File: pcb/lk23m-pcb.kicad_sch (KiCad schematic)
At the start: 59 parts, among them J1 Conn_01x02, SW1 RotaryEncoder_Switch_MP, SW10 SW_Push, SW11 SW_Push, SW12 SW_Push, SW13 SW_Push, SW14 SW_Push, SW15 SW_Push, SW16 SW_Push, SW17 SW_Push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

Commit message: Update LKBD libraries
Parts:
- H1, H2, H3, H4: value MountingHole -> MountingHole_Pad
- SW24: footprint LKBD_Common:SW_PUSH_1P1T_6x3.5mm -> LKBD_Common:SW_Push_1P1T_6x3.5mm
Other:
- moved on the sheet: H1, H2, H3, H4
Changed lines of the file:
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@@
 	)
 	(no_connect
-		(at 48.26 77.47)
+		(at 44.45 77.47)
 	)
 	(no_connect
@@
 	)
 	(no_connect
-		(at 26.67 77.47)
+		(at 20.32 77.47)
 	)
 	(no_connect
-		(at 91.44 77.47)
+		(at 92.71 77.47)
 	)
 	(no_connect
@@
 	)
 	(no_connect
-		(at 69.85 77.47)
+		(at 68.58 77.47)
 	)
 	(wire
@@
 	(symbol
 		(lib_id "Mechanical:MountingHole_Pad")
-		(at 69.85 74.93 0)
+		(at 68.58 74.93 0)
 		(unit 1)
 		(exclude_from_sim yes)
@@
 		(dnp no)
 		(property "Reference" "H3"
-			(at 72.39 73.6599 0)
+			(at 71.12 73.6599 0)
 			(effects
 				(font
@@
 			)
 		)
-		(property "Value" "MountingHole"
-			(at 72.39 76.1999 0)
+		(property "Value" "MountingHole_Pad"
+			(at 71.12 76.1999 0)
 			(effects
 				(font
@@
 		)
 		(property "Footprint" "MountingHole:MountingHole_2.2mm_M2_ISO14580_Pad"
-			(at 69.85 74.93 0)
+			(at 68.58 74.93 0)
 			(effects
 				(font
@@
 		)
 		(property "Datasheet" "~"
-			(at 69.85 74.93 0)
+			(at 68.58 74.93 0)
 			(effects
 				(font
@@
 		)
 		(property "Description" "Mounting Hole with connection"
-			(at 69.85 74.93 0)
+			(at 68.58 74.93 0)
 			(effects
 				(font
@@
 		)
 		(property "LCSC" ""
-			(at 69.85 74.93 0)
+			(at 68.58 74.93 0)
 			(effects
 				(font
@@
 		)
 		(property "JLC" ""
-			(at 69.85 74.93 0)
+			(at 68.58 74.93 0)
 			(effects
 				(font
@@
 		)
 		(property "JLCPosOffset" ""
-			(at 69.85 74.93 0)
+			(at 68.58 74.93 0)
 			(effects
 				(font
@@
 		)
 		(property "JLCRotOffset" ""
-			(at 69.85 74.93 0)
+			(at 68.58 74.93 0)
 			(effects
 				(font
@@
 	(symbol
 		(lib_id "Mechanical:MountingHole_Pad")
-		(at 26.67 74.93 0)
+		(at 20.32 74.93 0)
 		(unit 1)
 		(exclude_from_sim yes)
@@
 		(dnp no)
 		(property "Reference" "H1"
-			(at 29.21 73.66 0)
+			(at 22.86 73.66 0)
 			(effects
 				(font
@@
 			)
 		)
-		(property "Value" "MountingHole"
-			(at 29.21 76.2 0)
+		(property "Value" "MountingHole_Pad"
+			(at 22.86 76.2 0)
 			(effects
 				(font
@@
 		)
 		(property "Footprint" "MountingHole:MountingHole_2.2mm_M2_ISO14580_Pad"
-			(at 26.67 74.93 0)
+			(at 20.32 74.93 0)
 			(effects
 				(font
@@
 		)
 		(property "Datasheet" "~"
-			(at 26.67 74.93 0)
+			(at 20.32 74.93 0)
 			(effects
 				(font
@@
 		)
 		(property "Description" "Mounting Hole with connection"
-			(at 26.67 74.93 0)
+			(at 20.32 74.93 0)
 			(effects
 				(font
@@
 		)
 		(property "LCSC" ""
-			(at 26.67 74.93 0)
+			(at 20.32 74.93 0)
 			(effects
 				(font
@@
 		)
 		(property "JLC" ""
-			(at 26.67 74.93 0)
+			(at 20.32 74.93 0)
 			(effects
 				(font
@@
 		)
 		(property "JLCPosOffset" ""
-			(at 26.67 74.93 0)
+			(at 20.32 74.93 0)
 			(effects
 				(font
@@
 		)
 		(property "JLCRotOffset" ""
-			(at 26.67 74.93 0)
+			(at 20.32 74.93 0)
 			(effects
 				(font
@@
 	(symbol
 		(lib_id "Mechanical:MountingHole_Pad")
-		(at 91.44 74.93 0)
+		(at 92.71 74.93 0)
 		(unit 1)
 		(exclude_from_sim yes)
@@
 		(dnp no)
 		(property "Reference" "H4"
-			(at 93.98 73.66 0)
+			(at 95.25 73.66 0)
 			(effects
 				(font
@@
 			)
 		)
-		(property "Value" "MountingHole"
-			(at 93.98 76.2 0)
+		(property "Value" "MountingHole_Pad"
+			(at 95.25 76.2 0)
 			(effects
 				(font
@@
 		)
 		(property "Footprint" "MountingHole:MountingHole_2.2mm_M2_ISO14580_Pad"
-			(at 91.44 74.93 0)
+			(at 92.71 74.93 0)
 			(effects
 				(font
@@
 		)
 		(property "Datasheet" "~"
-			(at 91.44 74.93 0)
+			(at 92.71 74.93 0)
 			(effects
 				(font
@@
 		)
 		(property "Description" "Mounting Hole with connection"
-			(at 91.44 74.93 0)
+			(at 92.71 74.93 0)
 			(effects
 				(font
@@
 		)
 		(property "LCSC" ""
-			(at 91.44 74.93 0)
+			(at 92.71 74.93 0)
 			(effects
 				(font
@@
 		)
 		(property "JLC" ""
-			(at 91.44 74.93 0)
+			(at 92.71 74.93 0)
 			(effects
 				(font
@@
 		)
 		(property "JLCPosOffset" ""
-			(at 91.44 74.93 0)
+			(at 92.71 74.93 0)
 			(effects
 				(font
@@
 		)
 		(property "JLCRotOffset" ""
-			(at 91.44 74.93 0)
+			(at 92.71 74.93 0)
 			(effects
 				(font
@@
 			)
 		)
-		(property "Footprint" "LKBD_Common:SW_PUSH_1P1T_6x3.5mm"
+		(property "Footprint" "LKBD_Common:SW_Push_1P1T_6x3.5mm"
 			(at 38.1 88.9 0)
 			(effects
@@
 	(symbol
 		(lib_id "Mechanical:MountingHole_Pad")
-		(at 48.26 74.93 0)
+		(at 44.45 74.93 0)
 		(unit 1)
 		(exclude_from_sim yes)
@@
 		(dnp no)
 		(property "Reference" "H2"
-			(at 50.8 73.66 0)
+			(at 46.99 73.66 0)
 			(effects
 				(font
@@
 			)
 		)
-		(property "Value" "MountingHole"
-			(at 50.8 76.2 0)
+		(property "Value" "MountingHole_Pad"
+			(at 46.99 76.2 0)
 			(effects
 				(font
@@
 		)
 		(property "Footprint" "MountingHole:MountingHole_2.2mm_M2_ISO14580_Pad"
-			(at 48.26 74.93 0)
+			(at 44.45 74.93 0)
 			(effects
 				(font
@@
 		)
 		(property "Datasheet" "~"
-			(at 48.26 74.93 0)
+			(at 44.45 74.93 0)
 			(effects
 				(font
@@
 		)
 		(property "Description" "Mounting Hole with connection"
-			(at 48.26 74.93 0)
+			(at 44.45 74.93 0)
 			(effects
 				(font
@@
 		)
 		(property "LCSC" ""
-			(at 48.26 74.93 0)
+			(at 44.45 74.93 0)
 			(effects
 				(font
@@
 		)
 		(property "JLC" ""
-			(at 48.26 74.93 0)
+			(at 44.45 74.93 0)
 			(effects
 				(font
@@
 		)
 		(property "JLCPosOffset" ""
-			(at 48.26 74.93 0)
+			(at 44.45 74.93 0)
 			(effects
 				(font
@@
 		)
 		(property "JLCRotOffset" ""
-			(at 48.26 74.93 0)
+			(at 44.45 74.93 0)
 			(effects
 				(font
@@
 					(size 1.524 1.524)
 				)
+				(hide yes)
 			)
 		)

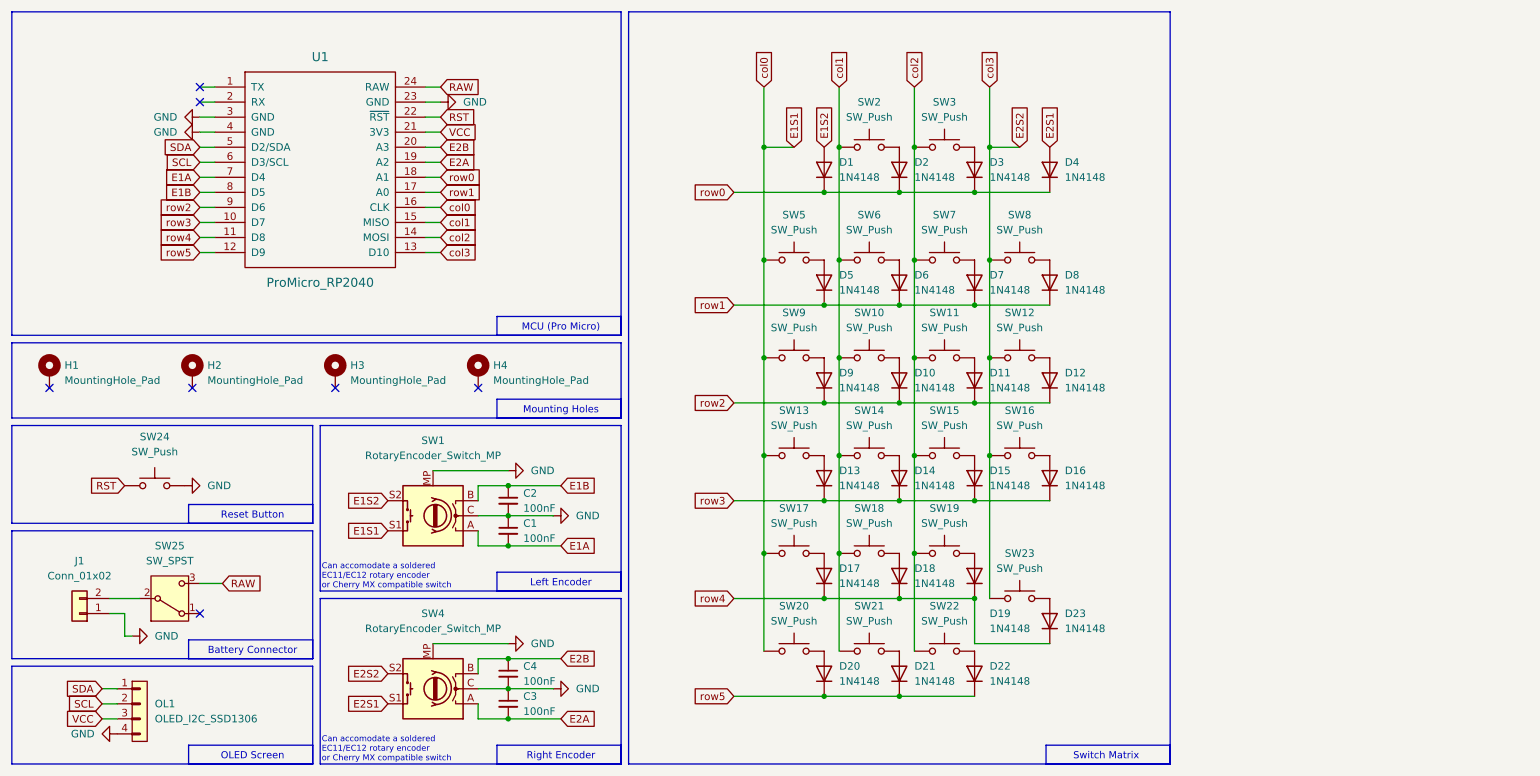
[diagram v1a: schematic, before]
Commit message: Update LICENSE document to Markdown
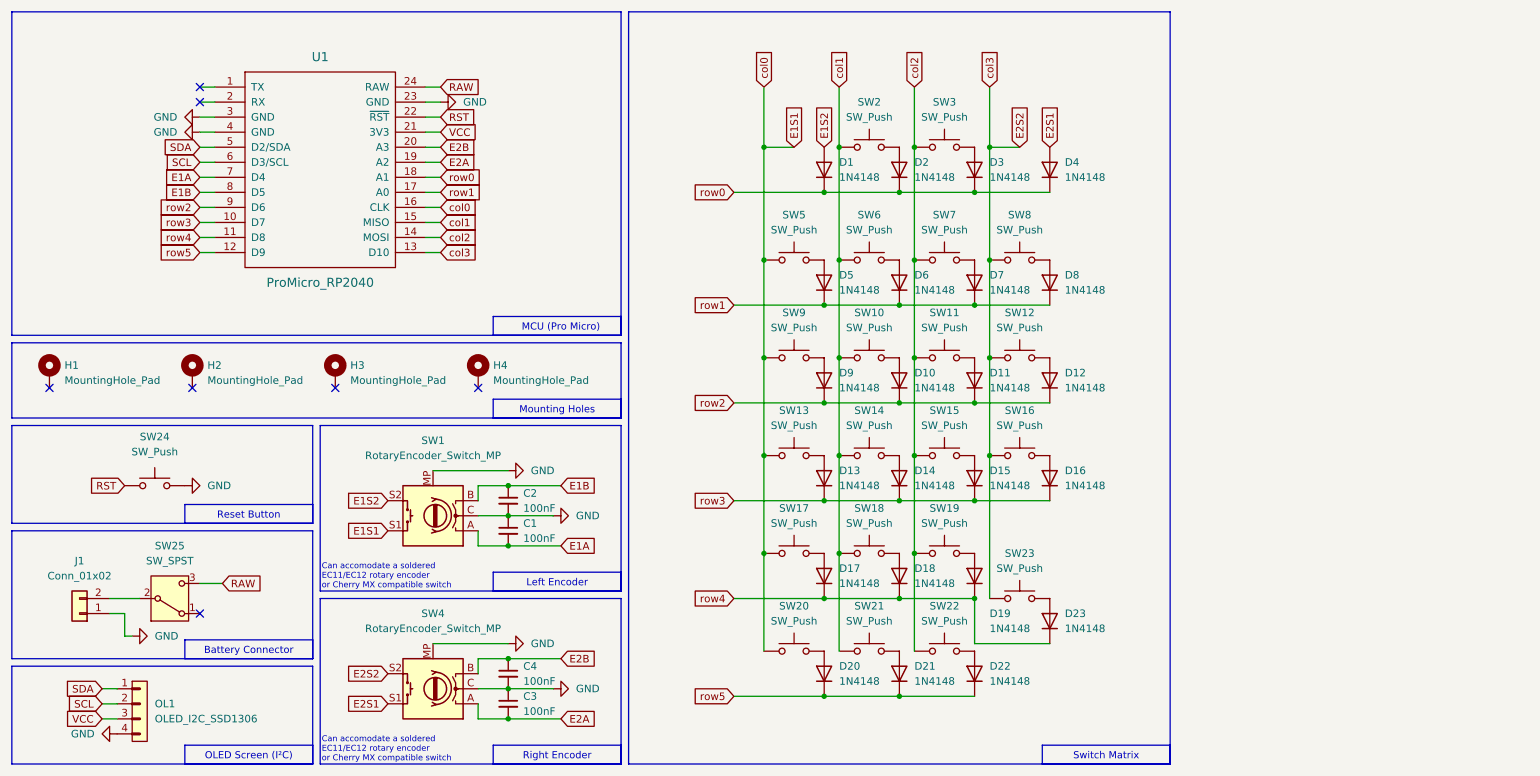
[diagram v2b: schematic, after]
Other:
- note added: "OLED Screen (I²C)"
- note removed: "OLED Screen"
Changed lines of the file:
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@@
+	)
+	(rectangle
+		(start 43.18 137.795)
+		(end 64.77 140.97)
+		(stroke
+			(width 0)
+			(type default)
+		)
+		(fill
+			(type none)
+		)
+	)
+	(rectangle
+		(start 95.25 108.585)
+		(end 116.84 111.76)
+		(stroke
+			(width 0)
+			(type default)
+		)
+		(fill
+			(type none)
+		)
+	)
+	(rectangle
+		(start 95.25 137.795)
+		(end 116.84 140.97)
+		(stroke
+			(width 0)
+			(type default)
+		)
+		(fill
+			(type none)
+		)
 	)
 	(rectangle
@@
 	)
 	(rectangle
-		(start 95.885 79.375)
+		(start 95.25 79.375)
 		(end 116.84 82.55)
 		(stroke
@@
 	)
 	(rectangle
-		(start 43.815 120.015)
-		(end 64.77 123.19)
-		(stroke
-			(width 0)
-			(type default)
-		)
-		(fill
-			(type none)
-		)
-	)
-	(rectangle
 		(start 13.97 13.97)
 		(end 116.84 68.58)
@@
 	)
 	(rectangle
-		(start 43.815 97.155)
+		(start 43.18 120.015)
+		(end 64.77 123.19)
+		(stroke
+			(width 0)
+			(type default)
+		)
+		(fill
+			(type none)
+		)
+	)
+	(rectangle
+		(start 43.18 97.155)
 		(end 64.77 100.33)
 		(stroke
@@
 	)
 	(rectangle
-		(start 188.595 137.795)
+		(start 187.96 137.795)
 		(end 209.55 140.97)
-		(stroke
-			(width 0)
-			(type default)
-		)
-		(fill
-			(type none)
-		)
-	)
-	(rectangle
-		(start 43.815 137.795)
-		(end 64.77 140.97)
 		(stroke
 			(width 0)
@@
 	)
 	(rectangle
-		(start 95.885 137.795)
-		(end 116.84 140.97)
-		(stroke
-			(width 0)
-			(type default)
-		)
-		(fill
-			(type none)
-		)
-	)
-	(rectangle
 		(start 13.97 83.82)
 		(end 64.77 100.33)
@@
 	)
 	(rectangle
-		(start 95.885 108.585)
-		(end 116.84 111.76)
-		(stroke
-			(width 0)
-			(type default)
-		)
-		(fill
-			(type none)
-		)
-	)
-	(rectangle
-		(start 95.885 65.405)
+		(start 95.25 65.405)
 		(end 116.84 68.58)
 		(stroke
@@
 	(text "Mounting Holes"
 		(exclude_from_sim no)
-		(at 106.68 81.28 0)
-		(effects
-			(font
-				(size 1.2 1.2)
-			)
-		)
-	)
-	(text "OLED Screen"
-		(exclude_from_sim no)
-		(at 54.61 139.7 0)
+		(at 106.045 81.28 0)
+		(effects
+			(font
+				(size 1.2 1.2)
+			)
+		)
+	)
+	(text "OLED Screen (I²C)"
+		(exclude_from_sim no)
+		(at 53.975 139.7 0)
 		(effects
 			(font
@@
 	(text "Reset Button"
 		(exclude_from_sim no)
-		(at 54.61 99.06 0)
+		(at 53.975 99.06 0)
 		(effects
 			(font
@@
 	(text "Right Encoder"
 		(exclude_from_sim no)
-		(at 106.68 139.7 0)
+		(at 106.045 139.7 0)
 		(effects
 			(font
@@
 	(text "Left Encoder"
 		(exclude_from_sim no)
-		(at 106.68 110.49 0)
+		(at 106.045 110.49 0)
 		(effects
 			(font
@@
 	(text "Battery Connector"
 		(exclude_from_sim no)
-		(at 54.61 121.92 0)
-		(effects
-			(font
+		(at 53.975 121.92 0)
+		(effects
+			(font

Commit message: Use a JST-PH Right Angle connector for battery
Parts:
- J1: footprint Connector_JST:JST_PH_B2B-PH-K_1x02_P2.00mm_Vertical -> Connector_JST:JST_PH_S2B-PH-K_1x02_P2.00mm_Horizontal
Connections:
- net E1S1 renamed col0
- net E2S2 renamed col3
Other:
- note added: "ONLY USE THE BATTERY CONNECTOR FOR CONTROLER ALLOWING POWER INPUT VIA THE RAW PIN AND THAT PROVIDES A ONBOARD CHARGING CIRCUIT SUCH AS THE nice!nano."
- moved on the sheet: J1, OL1, SW24, SW25
